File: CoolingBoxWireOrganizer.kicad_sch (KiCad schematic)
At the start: 67 parts, among them J1 Conn_02x02_Odd_Even, J10 Conn_01x08_Pin, J11 Conn_02x02_Odd_Even, J12 Conn_02x03_Odd_Even, J13 Conn_01x08_Pin, J14 Conn_01x02, J15 Conn_02x18_Odd_Even, J16 Conn_02x02_Odd_Even, J17 Conn_01x02, J18 DILB16P-223TLF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

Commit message: trying to change chiller curcuit(on progress)
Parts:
- added D? (x2): D, Diode_SMD:D_0603_1608Metric_Pad1.05x0.95mm_HandSolder, symbol Device:D
- added J? (x2): Conn_01x02, symbol Connector_Generic:Conn_01x02
- added J?: Conn_01x04, symbol Connector_Generic:Conn_01x04
- added R?: 1000, Resistor_SMD:R_0603_1608Metric_Pad0.98x0.95mm_HandSolder, symbol Device:R
- added R?: 10000, Resistor_SMD:R_0603_1608Metric_Pad0.98x0.95mm_HandSolder, symbol Device:R
- added R?: 3900, Resistor_SMD:R_0603_1608Metric_Pad0.98x0.95mm_HandSolder, symbol Device:R
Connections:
- net Chiller.Alarm.GND: now also J?.2 (Pin_2)
- net Chiller.Alarm.Sig: now also R?.1, R?.2
- net Chiller.Alarm.input: now also J?.3 (Pin_3)
- net GND: now also J?.1 (Pin_1), R?.1
- net SSR.GND: now also D?.1 (K), D?.2 (A), J?.2 (Pin_2)
- net to chiller alarm relay: now also J?.1 (Pin_1), R?.2
- new net: D?.1 (K), D?.2 (A), R?.1
- new net: J?.2 (Pin_2), R?.2
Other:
- moved on the sheet: D3, D5, J20, R1, R2, R20

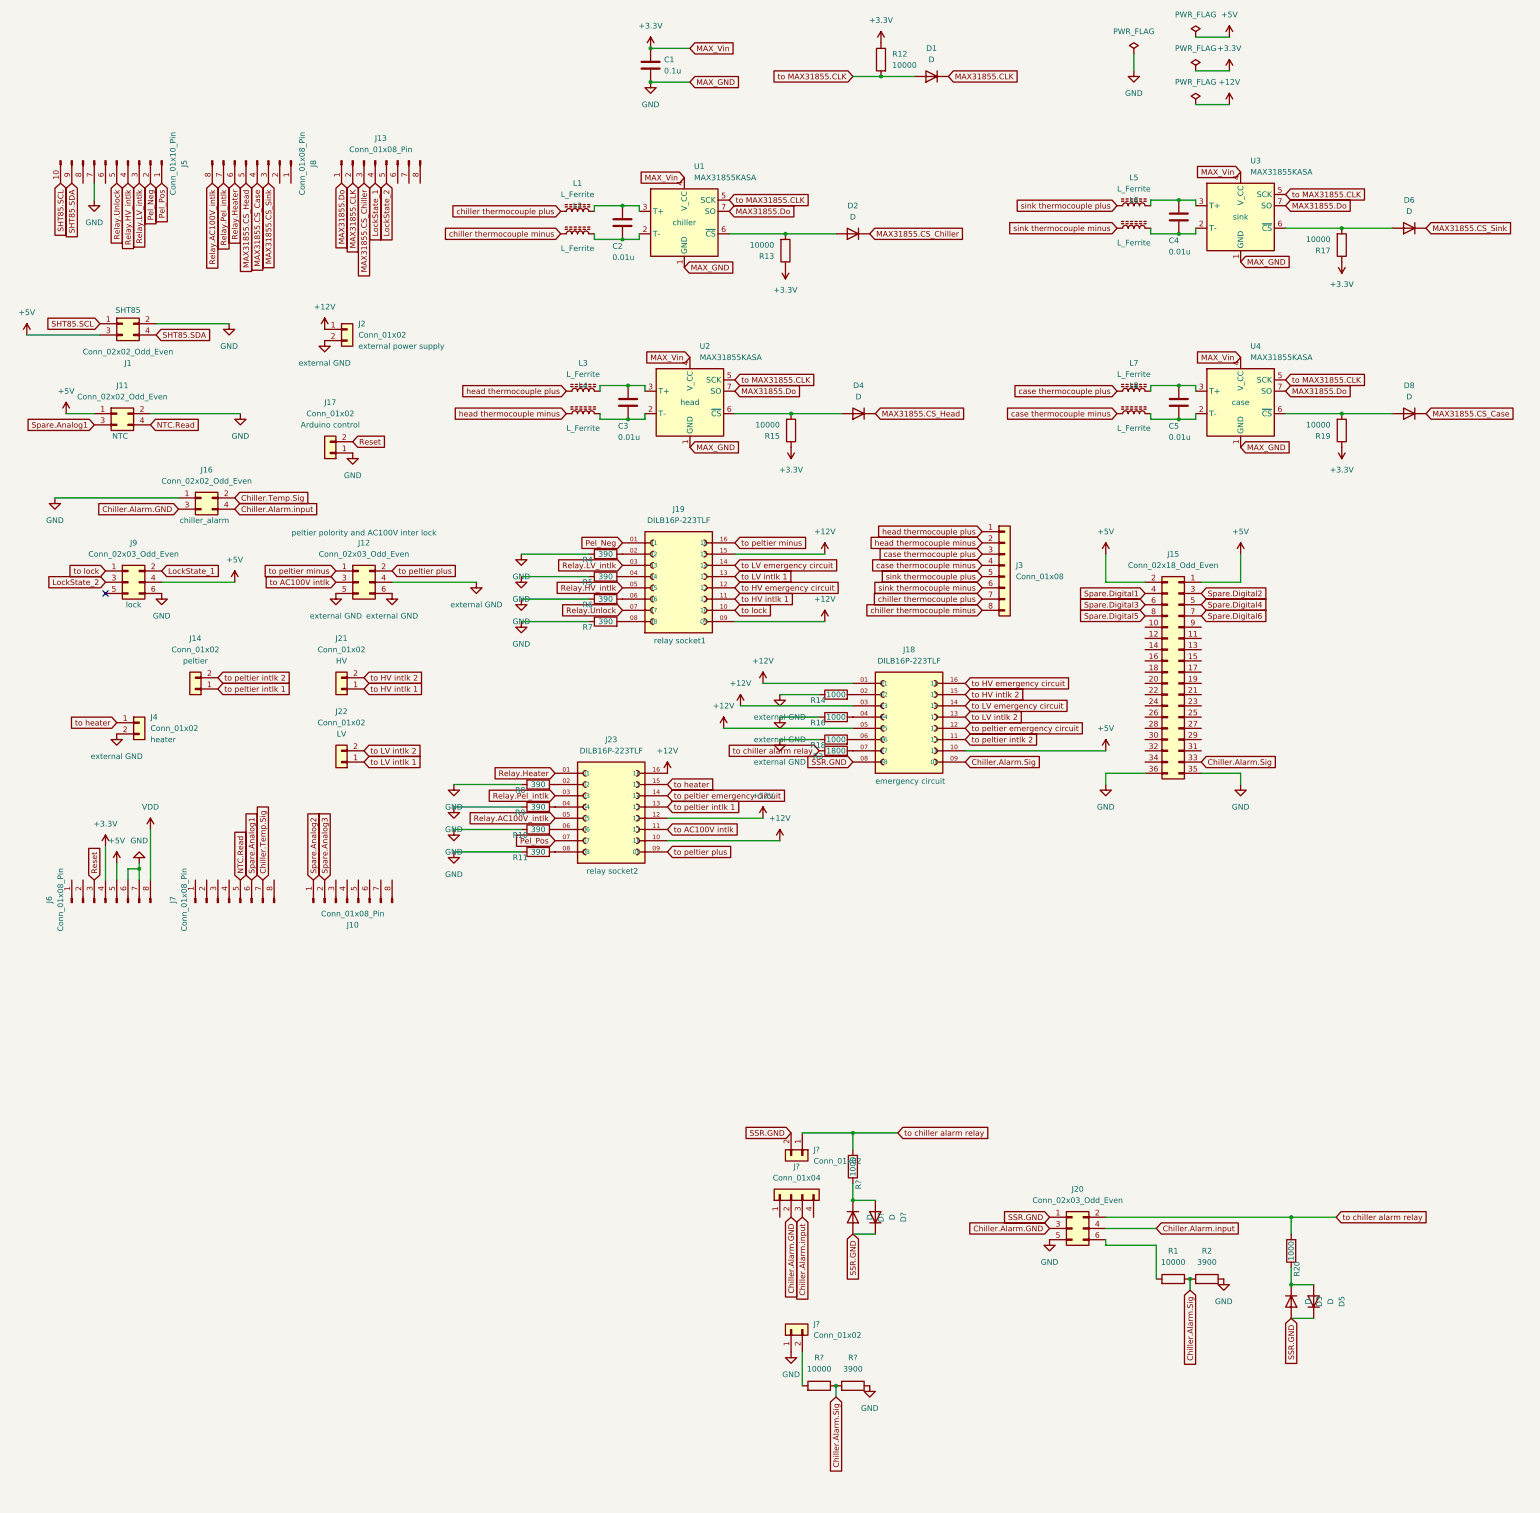
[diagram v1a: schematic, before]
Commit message: Added jumper pins to bom. To realize GND isolation, fixed chiller alarm circuit. And fixed silk.
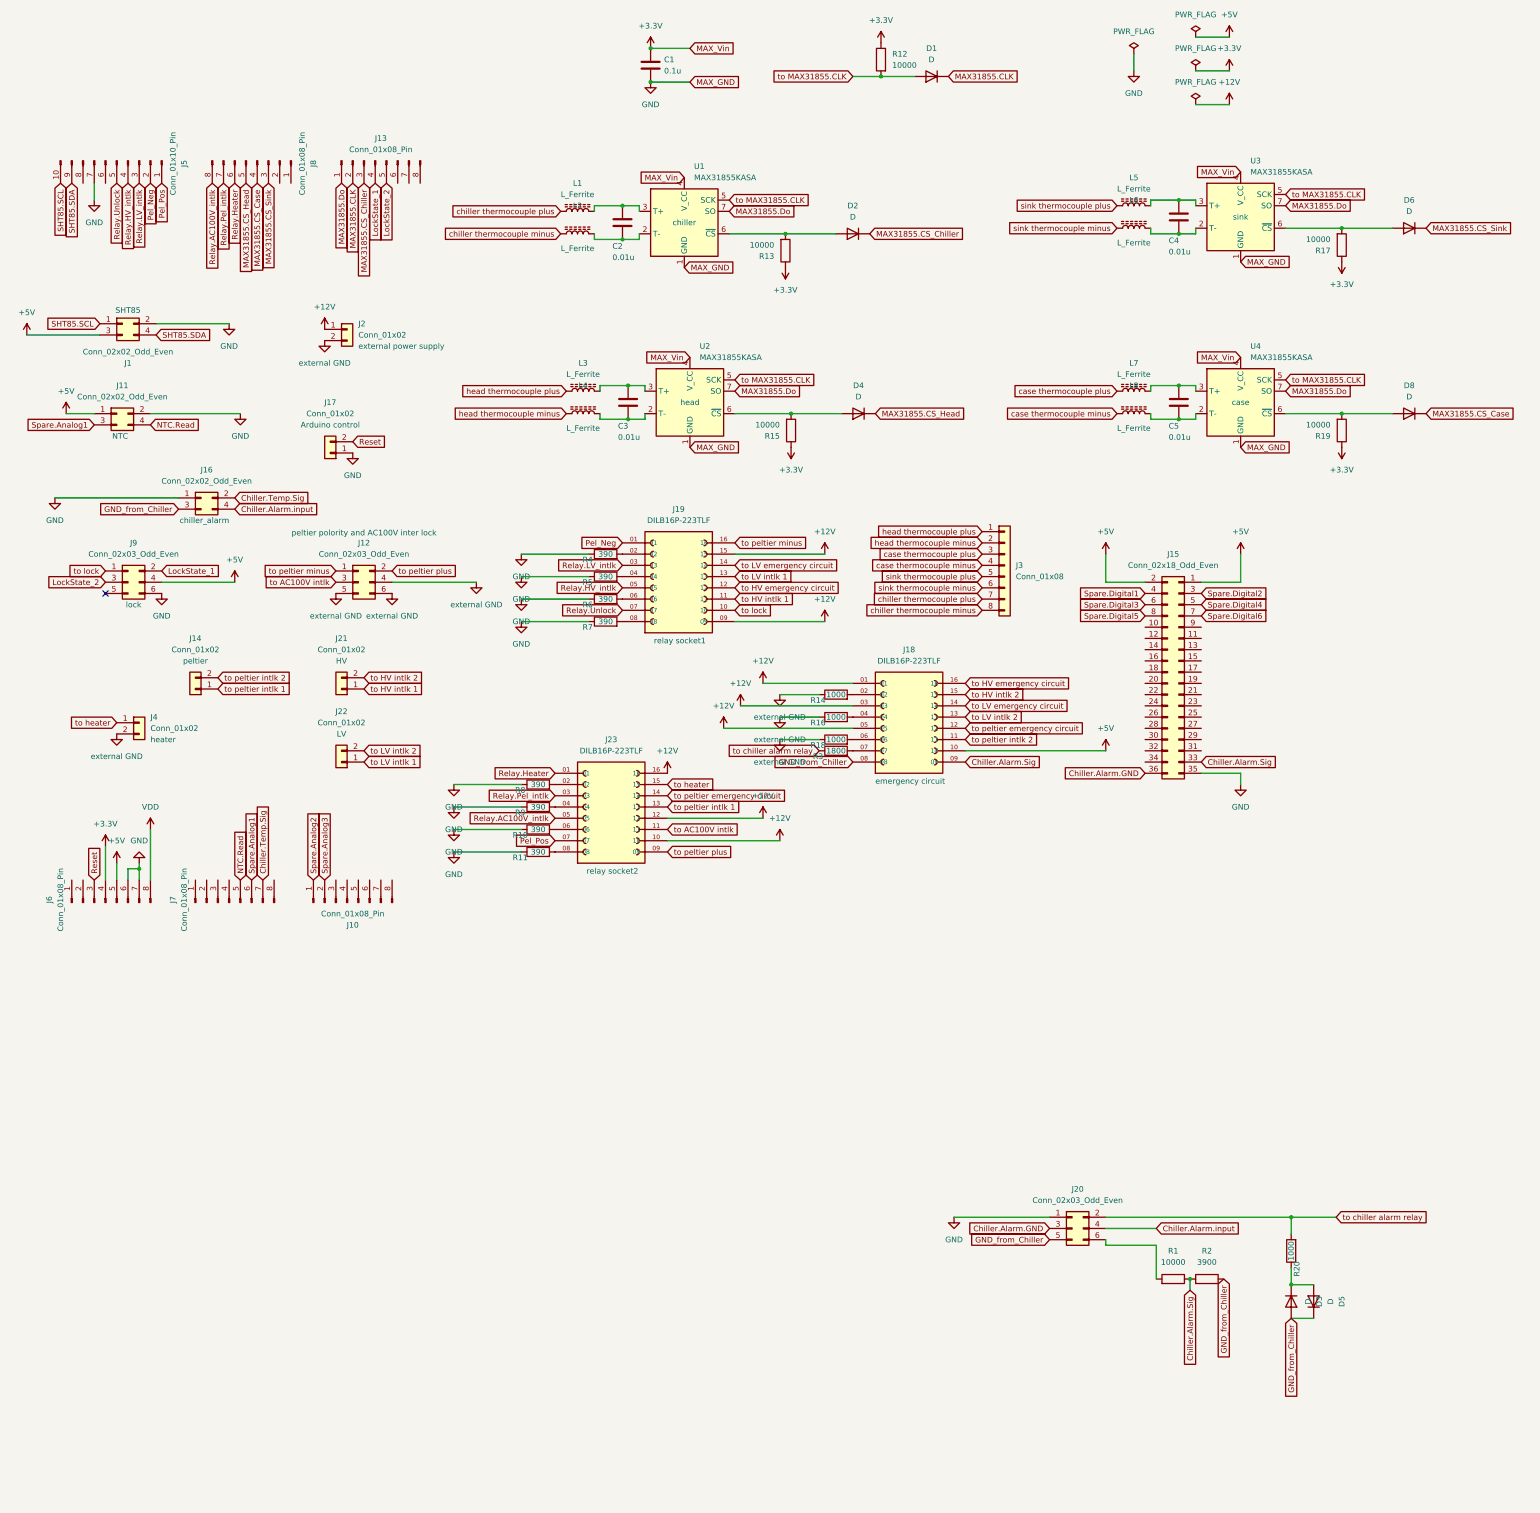
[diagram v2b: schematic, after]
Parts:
- removed D? (x2): D, Diode_SMD:D_0603_1608Metric_Pad1.05x0.95mm_HandSolder, symbol Device:D
- removed J? (x2): Conn_01x02, symbol Connector_Generic:Conn_01x02
- removed J?: Conn_01x04, symbol Connector_Generic:Conn_01x04
- removed R?: 1000, Resistor_SMD:R_0603_1608Metric_Pad0.98x0.95mm_HandSolder, symbol Device:R
- removed R?: 10000, Resistor_SMD:R_0603_1608Metric_Pad0.98x0.95mm_HandSolder, symbol Device:R
- removed R?: 3900, Resistor_SMD:R_0603_1608Metric_Pad0.98x0.95mm_HandSolder, symbol Device:R
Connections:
- net Chiller.Alarm.GND: now also J15.36 (Pin_36); no longer J16.3 (Pin_3)
- net GND: now also J20.1 (Pin_1); no longer J15.36 (Pin_36), J20.5 (Pin_5), R2.1
- net SSR.GND renamed GND_from_Chiller
- net GND_from_Chiller: now also J16.3 (Pin_3), J20.5 (Pin_5), R2.1; no longer J20.1 (Pin_1)
